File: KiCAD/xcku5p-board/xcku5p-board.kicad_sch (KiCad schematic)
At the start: 0 parts

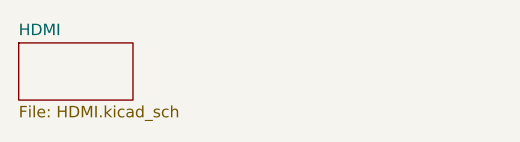
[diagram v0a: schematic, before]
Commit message: Add SD card circuit
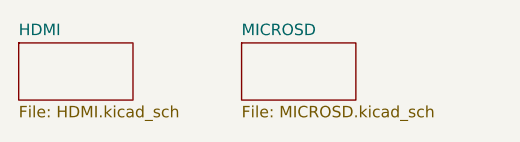
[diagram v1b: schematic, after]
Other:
- added sheet MICROSD (MICROSD.kicad_sch)
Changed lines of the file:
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@@
+		)
+	)
+	(sheet
+		(at 48.895 22.86)
+		(size 12.7 6.35)
+		(exclude_from_sim no)
+		(in_bom yes)
+		(on_board yes)
+		(dnp no)
+		(fields_autoplaced yes)
+		(stroke
+			(width 0.1524)
+			(type solid)
+		)
+		(fill
+			(color 0 0 0 0)
+		)
+		(property "Sheetname" "MICROSD"
+			(at 48.895 22.1484 0)
+			(show_name no)
+			(do_not_autoplace no)
+			(effects
+				(font
+					(size 1.27 1.27)
+				)
+				(justify left bottom)
+			)
+		)
+		(property "Sheetfile" "MICROSD.kicad_sch"
+			(at 48.895 29.7946 0)
+			(show_name no)
+			(do_not_autoplace no)
+			(effects
+				(font
+					(size 1.27 1.27)
+				)
+				(justify left top)
+			)
+		)
+		(instances
+			(project "xcku5p-board"
+				(path "/c44d7773-a123-40d0-b8be-ab612fbc35da"
+					(page "3")
+				)
+			)
 		)
 	)

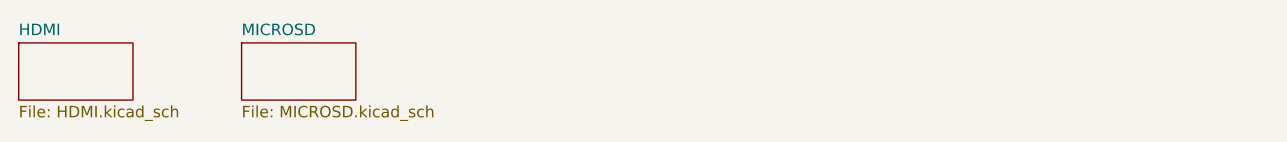
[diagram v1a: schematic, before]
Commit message: Add power circuit, switches, UART bridge
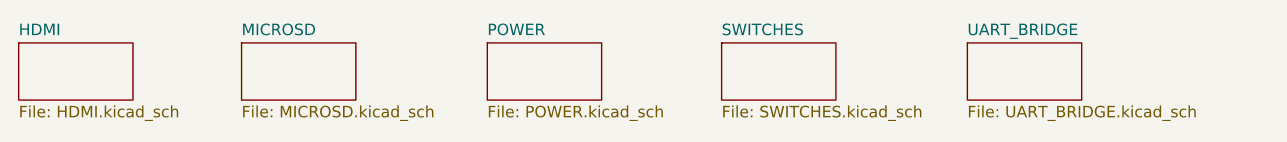
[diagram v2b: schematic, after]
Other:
- added sheet POWER (POWER.kicad_sch)
- added sheet SWITCHES (SWITCHES.kicad_sch)
- added sheet UART_BRIDGE (UART_BRIDGE.kicad_sch)
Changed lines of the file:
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@@
 	(paper "A4")
+	(sheet
+		(at 129.54 22.86)
+		(size 12.7 6.35)
+		(exclude_from_sim no)
+		(in_bom yes)
+		(on_board yes)
+		(dnp no)
+		(fields_autoplaced yes)
+		(stroke
+			(width 0.1524)
+			(type solid)
+		)
+		(fill
+			(color 0 0 0 0)
+		)
+		(property "Sheetname" "UART_BRIDGE"
+			(at 129.54 22.1484 0)
+			(show_name no)
+			(do_not_autoplace no)
+			(effects
+				(font
+					(size 1.27 1.27)
+				)
+				(justify left bottom)
+			)
+		)
+		(property "Sheetfile" "UART_BRIDGE.kicad_sch"
+			(at 129.54 29.7946 0)
+			(show_name no)
+			(do_not_autoplace no)
+			(effects
+				(font
+					(size 1.27 1.27)
+				)
+				(justify left top)
+			)
+		)
+		(instances
+			(project "xcku5p-board"
+				(path "/c44d7773-a123-40d0-b8be-ab612fbc35da"
+					(page "6")
+				)
+			)
+		)
+	)
+	(sheet
+		(at 76.2 22.86)
+		(size 12.7 6.35)
+		(exclude_from_sim no)
+		(in_bom yes)
+		(on_board yes)
+		(dnp no)
+		(fields_autoplaced yes)
+		(stroke
+			(width 0.1524)
+			(type solid)
+		)
+		(fill
+			(color 0 0 0 0)
+		)
+		(property "Sheetname" "POWER"
+			(at 76.2 22.1484 0)
+			(show_name no)
+			(do_not_autoplace no)
+			(effects
+				(font
+					(size 1.27 1.27)
+				)
+				(justify left bottom)
+			)
+		)
+		(property "Sheetfile" "POWER.kicad_sch"
+			(at 76.2 29.7946 0)
+			(show_name no)
+			(do_not_autoplace no)
+			(effects
+				(font
+					(size 1.27 1.27)
+				)
+				(justify left top)
+			)
+		)
+		(instances
+			(project "xcku5p-board"
+				(path "/c44d7773-a123-40d0-b8be-ab612fbc35da"
+					(page "4")
+				)
+			)
+		)
+	)
 	(sheet
 		(at 24.13 22.86)
@@
 				)
 			)
+		)
+	)
+	(sheet
+		(at 102.235 22.86)
+		(size 12.7 6.35)
+		(exclude_from_sim no)
+		(in_bom yes)
+		(on_board yes)
+		(dnp no)
+		(fields_autoplaced yes)
+		(stroke
+			(width 0.1524)
+			(type solid)
+		)
+		(fill
+			(color 0 0 0 0)
+		)
+		(property "Sheetname" "SWITCHES"
+			(at 102.235 22.1484 0)
+			(show_name no)
+			(do_not_autoplace no)
+			(effects
+				(font
+					(size 1.27 1.27)
+				)
+				(justify left bottom)
+			)
+		)
+		(property "Sheetfile" "SWITCHES.kicad_sch"
+			(at 102.235 29.7946 0)
+			(show_name no)
+			(do_not_autoplace no)
+			(effects
+				(font
+					(size 1.27 1.27)
+				)
+				(justify left top)
+			)
+		)
+		(instances
+			(project "xcku5p-board"
+				(path "/c44d7773-a123-40d0-b8be-ab612fbc35da"
+					(page "5")
+				)
+			)
